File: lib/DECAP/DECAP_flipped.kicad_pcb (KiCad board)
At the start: 2 copper layers, 1 part

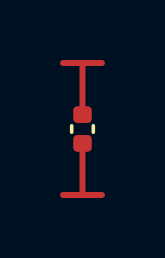
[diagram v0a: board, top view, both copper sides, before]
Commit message: All cells now use 1mm*4mm grid rather than 1.1mm*4.4mm
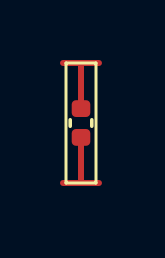
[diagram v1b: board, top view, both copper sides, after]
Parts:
- moved C 0.21 mm to (0.50, 2.00)
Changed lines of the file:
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@@
 	(footprint "Capacitor_SMD:C_0402_1005Metric"
 		(layer "F.Cu")
-		(at 0.55 2.2 -90)
+		(at 0.5 2 -90)
 		(descr "Capacitor SMD 0402 (1005 Metric), square (rectangular) end terminal, IPC-7351 nominal, (Body size source: IPC-SM-782 page 76, https://www.pcb-3d.com/wordpress/wp-content/uploads/ipc-sm-782a_amendment_1_and_2.pdf), generated with kicad-footprint-generator")
 		(tags "capacitor")
@@
 			)
 			(layer "F.SilkS")
+			(net 15)
 		)
 		(fp_line
@@
 			)
 			(layer "F.SilkS")
+			(net 15)
 		)
 		(fp_line
@@
 			)
 			(layer "F.CrtYd")
+			(net 15)
 		)
 		(fp_line
@@
 			)
 			(layer "F.CrtYd")
+			(net 15)
 		)
 		(fp_line
@@
 			)
 			(layer "F.CrtYd")
+			(net 15)
 		)
 		(fp_line
@@
 			)
 			(layer "F.CrtYd")
+			(net 15)
 		)
 		(fp_line
@@
 			)
 			(layer "F.Fab")
+			(net 15)
 		)
 		(fp_line
@@
 			)
 			(layer "F.Fab")
+			(net 15)
 		)
 		(fp_line
@@
 			)
 			(layer "F.Fab")
+			(net 15)
 		)
 		(fp_line
@@
 			)
 			(layer "F.Fab")
+			(net 15)
 		)
 		(fp_text user "${REFERENCE}"
@@
 		)
 	)
-	(gr_line
-		(start 1.1 4.4)
-		(end 0 4.4)
-		(stroke
-			(width 0.1)
-			(type default)
-		)
-		(layer "F.Fab")
-	)
-	(gr_line
+	(gr_rect
+		(start 0 0)
+		(end 1 4)
+		(stroke
+			(width 0.1)
+			(type default)
+		)
+		(fill no)
+		(layer "F.SilkS")
+	)
+	(gr_line
+		(start 0 4)
+		(end 0 0)
+		(stroke
+			(width 0.1)
+			(type default)
+		)
+		(layer "F.Fab")
+	)
+	(gr_line
+		(start 1 0)
+		(end 1 4)
+		(stroke
+			(width 0.1)
+			(type default)
+		)
+		(layer "F.Fab")
+	)
+	(gr_line
+		(start 1 4)
+		(end 0 4)
+		(stroke
+			(width 0.1)
+			(type default)
+		)
+		(layer "F.Fab")
+	)
+	(gr_line
+		(start -0.1 0)
+		(end 1 0)
+		(stroke
+			(width 0.1)
+			(type default)
+		)
+		(layer "F.Fab")
+	)
+	(segment
 		(start 1.1 0)
-		(end 1.1 4.4)
-		(stroke
-			(width 0.1)
-			(type default)
-		)
-		(layer "F.Fab")
-	)
-	(gr_line
-		(start 0 0)
-		(end 1.1 0)
-		(stroke
-			(width 0.1)
-			(type default)
-		)
-		(layer "F.Fab")
-	)
-	(gr_line
-		(start 0 4.4)
-		(end 0 0)
-		(stroke
-			(width 0.1)
-			(type default)
-		)
-		(layer "F.Fab")
-	)
-	(segment
-		(start 0.55 1.72)
-		(end 0.55 0.05)
+		(end 0.5 0)
 		(width 0.2)
 		(layer "F.Cu")
@@
 	)
 	(segment
-		(start 1.2 0)
+		(start 0.5 0)
 		(end -0.1 0)
 		(width 0.2)
@@
 	)
 	(segment
-		(start 0.55 0.05)
+		(start 0.5 1.52)
 		(end 0.5 0)
 		(width 0.2)
@@
 	)
 	(segment
-		(start 0.55 2.68)
-		(end 0.55 4.35)
+		(start 1.1 4)
+		(end 0.5 4)
 		(width 0.2)
 		(layer "F.Cu")
@@
 	)
 	(segment
-		(start 1.2 4.4)
-		(end -0.1 4.4)
+		(start 0.5 4)
+		(end -0.1 4)
 		(width 0.2)
 		(layer "F.Cu")
@@
 	)
 	(segment
-		(start 0.55 4.35)
-		(end 0.6 4.4)
-		(width 0.2)
-		(layer "F.Cu")
+		(start 0.5 2.48)
+		(end 0.5 4)
+		(width 0.2)
+		(layer "F.Cu")

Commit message: Set value of decap
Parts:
- C: value (none) -> 0.1u
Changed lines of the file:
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@@
 			)
 		)
-		(property "Value" ""
+		(property "Value" "0.1u"
 			(at 0 1.16 90)
 			(layer "F.Fab")
@@
 			)
 			(layer "F.SilkS")
-			(net 15)
 		)
 		(fp_line
@@
 			)
 			(layer "F.SilkS")
-			(net 15)
 		)
 		(fp_line
@@
 			)
 			(layer "F.CrtYd")
-			(net 15)
 		)
 		(fp_line
@@
 			)
 			(layer "F.CrtYd")
-			(net 15)
 		)
 		(fp_line
@@
 			)
 			(layer "F.CrtYd")
-			(net 15)
 		)
 		(fp_line
@@
 			)
 			(layer "F.CrtYd")
-			(net 15)
 		)
 		(fp_line
@@
 			)
 			(layer "F.Fab")
-			(net 15)
 		)
 		(fp_line
@@
 			)
 			(layer "F.Fab")
-			(net 15)
 		)
 		(fp_line
@@
 			)
 			(layer "F.Fab")
-			(net 15)
 		)
 		(fp_line
@@
 			)
 			(layer "F.Fab")
-			(net 15)
 		)
 		(fp_text user "${REFERENCE}"
